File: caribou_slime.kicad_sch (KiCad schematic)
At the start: 36 parts, among them J1 BATT JST, Q1 AO3145, U1 ESP32-C3_SUPERMINI, U2 BMI270, U3 FS312F-G, U4 FS8205A, U5 TP4056, U6 ME6211C33M5G

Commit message: fix(pcb): Move S1A to enable pin of regulator
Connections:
- net VUNREG: now also S1.2 (B); no longer S1.1 (A)
- net at U6.3 (EN): now also S1.1 (A); no longer S1.2 (B)
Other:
- moved on the sheet: S1A

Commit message: fix(schematic): Add pulldown to regulator EN pin
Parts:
- added R17: 10k, Resistor_SMD:R_0805_2012Metric, symbol Device:R
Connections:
- net GND: now also R17.2
- net at S1.1 (A), U6.3 (EN): now also R17.1
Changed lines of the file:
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@@
   (junction (at 252.73 93.98) (diameter 0) (color 0 0 0 0)
   )
+  (junction (at 234.95 82.55) (diameter 0) (color 0 0 0 0)
+  )
   (junction (at 48.26 161.29) (diameter 0) (color 0 0 0 0)
   )
@@
   )
   (junction (at 113.03 143.51) (diameter 0) (color 0 0 0 0)
+  )
+  (junction (at 247.65 72.39) (diameter 0) (color 0 0 0 0)
   )
   (no_connect (at 77.47 171.45))
@@
     (stroke (width 0) (type default))
   )
+  (wire (pts (xy 247.65 72.39) (xy 234.95 72.39))
+    (stroke (width 0) (type default))
+  )
   (wire (pts (xy 72.39 153.67) (xy 77.47 153.67))
     (stroke (width 0) (type default))
@@
     (stroke (width 0) (type default))
   )
+  (wire (pts (xy 234.95 81.28) (xy 234.95 82.55))
+    (stroke (width 0) (type default))
+  )
   (wire (pts (xy 16.51 81.28) (xy 53.34 81.28))
     (stroke (width 0) (type default))
@@
   )
   (wire (pts (xy 154.94 71.12) (xy 154.94 72.39))
+    (stroke (width 0) (type default))
+  )
+  (wire (pts (xy 234.95 72.39) (xy 234.95 73.66))
     (stroke (width 0) (type default))
   )
@@
         )
       )
+    )
+  )
+  (symbol (lib_id "Device:R") (at 234.95 77.47 0) (mirror y) (unit 1)
+    (in_bom yes) (on_board yes) (dnp no)
+    (property "Reference" "R17" (at 232.41 76.2 0)
+      (effects (font (size 1.27 1.27)) (justify left))
+    )
+    (property "Value" "10k" (at 232.41 78.74 0)
+      (effects (font (size 1.27 1.27)) (justify left))
+    )
+    (property "Footprint" "Resistor_SMD:R_0805_2012Metric" (at 236.728 77.47 90)
+      (effects (font (size 1.27 1.27)) hide)
+    )
+    (property "Datasheet" "~" (at 234.95 77.47 0)
+      (effects (font (size 1.27 1.27)) hide)
+    )
+    (pin "1")
+    (pin "2")
+    (instances
+      (project "caribou_slime"
+        (path "/61bfc64c-87c3-434a-8ade-1f9e7b05e459"
+          (reference "R17") (unit 1)
+        )
+      )

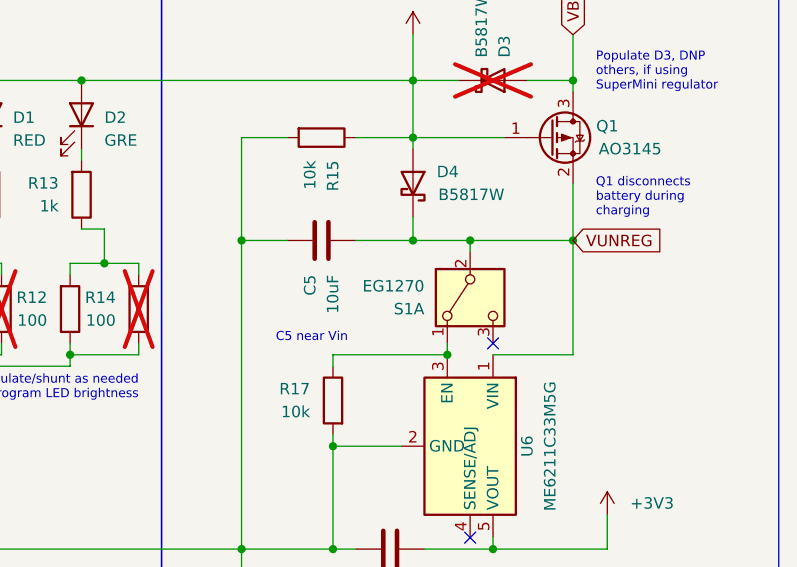
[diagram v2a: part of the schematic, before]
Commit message: refactor(schematic): Rework S1A to disconnect pulldown when reg en high
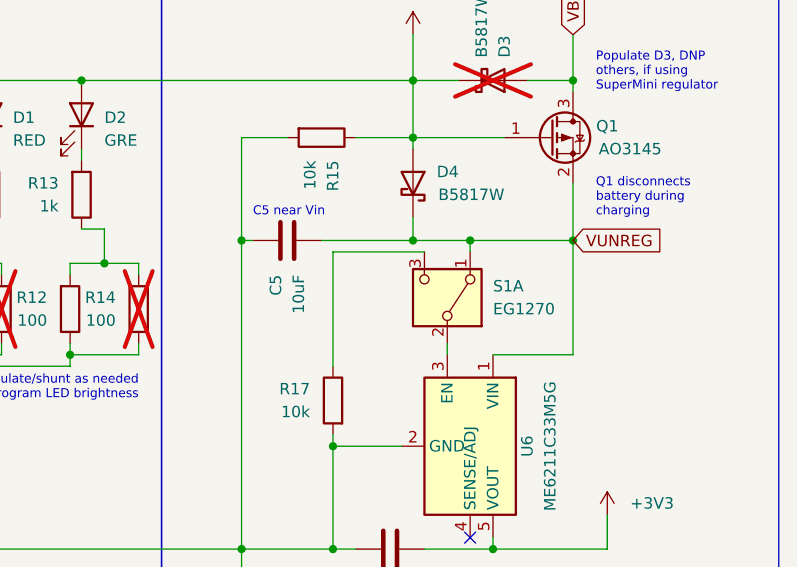
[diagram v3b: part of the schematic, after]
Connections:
- net VUNREG: now also S1.1 (A); no longer S1.2 (B)
- net at S1.3 (C): now also R17.1
- new net: S1.2 (B), U6.3 (EN)
- no-connect marks 19 -> 18
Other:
- moved on the sheet: C5, S1A
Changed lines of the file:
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@@
   (junction (at 113.03 143.51) (diameter 0) (color 0 0 0 0)
-  )
-  (junction (at 247.65 72.39) (diameter 0) (color 0 0 0 0)
   )
   (no_connect (at 77.47 171.45))
@@
   (no_connect (at 71.12 64.77))
   (no_connect (at 107.95 171.45))
-  (no_connect (at 252.73 71.12))
   (no_connect (at 71.12 57.15))
   (no_connect (at 77.47 151.13))
@@
   (no_connect (at 107.95 168.91))
   (no_connect (at 101.6 34.29))
+  (wire (pts (xy 245.11 60.96) (xy 234.95 60.96))
+    (stroke (width 0) (type default))
+  )
   (wire (pts (xy 224.79 59.69) (xy 224.79 93.98))
     (stroke (width 0) (type default))
@@
     (stroke (width 0) (type default))
   )
-  (wire (pts (xy 247.65 72.39) (xy 234.95 72.39))
-    (stroke (width 0) (type default))
-  )
   (wire (pts (xy 72.39 153.67) (xy 77.47 153.67))
     (stroke (width 0) (type default))
@@
     (stroke (width 0) (type default))
   )
-  (wire (pts (xy 243.84 59.69) (xy 237.49 59.69))
+  (wire (pts (xy 243.84 59.69) (xy 233.68 59.69))
     (stroke (width 0) (type default))
   )
@@
     (stroke (width 0) (type default))
   )
-  (wire (pts (xy 229.87 59.69) (xy 224.79 59.69))
+  (wire (pts (xy 226.06 59.69) (xy 224.79 59.69))
     (stroke (width 0) (type default))
   )
@@
     (stroke (width 0) (type default))
   )
-  (wire (pts (xy 234.95 72.39) (xy 234.95 73.66))
+  (wire (pts (xy 234.95 60.96) (xy 234.95 73.66))
     (stroke (width 0) (type default))
   )
@@
     (effects (font (size 1 1)) (justify left bottom))
   )
-  (text "C5 near Vin" (at 228.6 71.12 0)
+  (text "C5 near Vin" (at 226.06 57.15 0)
     (effects (font (size 1 1)) (justify left bottom))
   )
@@
     )
   )
-  (symbol (lib_id "Device:C") (at 233.68 59.69 90) (mirror x) (unit 1)
-    (in_bom yes) (on_board yes) (dnp no) (fields_autoplaced)
-    (property "Reference" "C5" (at 232.41 63.5 0)
+  (symbol (lib_id "Device:C") (at 229.87 59.69 90) (mirror x) (unit 1)
+    (in_bom yes) (on_board yes) (dnp no) (fields_autoplaced)
+    (property "Reference" "C5" (at 228.6 63.5 0)
       (effects (font (size 1.27 1.27)) (justify left))
     )
-    (property "Value" "10uF" (at 234.95 63.5 0)
+    (property "Value" "10uF" (at 231.14 63.5 0)
       (effects (font (size 1.27 1.27)) (justify left))
     )
-    (property "Footprint" "Capacitor_SMD:C_0805_2012Metric" (at 237.49 60.6552 0)
-      (effects (font (size 1.27 1.27)) hide)
-    )
-    (property "Datasheet" "~" (at 233.68 59.69 0)
+    (property "Footprint" "Capacitor_SMD:C_0805_2012Metric" (at 233.68 60.6552 0)
+      (effects (font (size 1.27 1.27)) hide)
+    )
+    (property "Datasheet" "~" (at 229.87 59.69 0)
       (effects (font (size 1.27 1.27)) hide)
     )
@@
     )
   )
-  (symbol (lib_id "Switch:SW_DPDT_x2") (at 250.19 66.04 90) (mirror x) (unit 1)
+  (symbol (lib_id "Switch:SW_DPDT_x2") (at 247.65 66.04 270) (mirror x) (unit 1)
     (in_bom yes) (on_board yes) (dnp no)
-    (property "Reference" "S1" (at 245.11 67.31 90)
+    (property "Reference" "S1" (at 252.73 64.77 90)
       (effects (font (size 1.27 1.27)) (justify left))
     )
-    (property "Value" "EG1270" (at 245.11 64.77 90)
+    (property "Value" "EG1270" (at 252.73 67.31 90)
       (effects (font (size 1.27 1.27)) (justify left))
     )
-    (property "Footprint" "EG1270:SW_EG1270" (at 250.19 66.04 0)
-      (effects (font (size 1.27 1.27)) hide)
-    )
-    (property "Datasheet" "~" (at 250.19 66.04 0)
-      (effects (font (size 1.27 1.27)) hide)
-    )
+    (property "Footprint" "EG1270:SW_EG1270" (at 247.65 66.04 0)
+      (effects (font (size 1.27 1.27)) hide)
+    )
+    (property "Datasheet" "~" (at 247.65 66.04 0)
+      (effects (font (size 1.27 1.27)) hide)
+    )

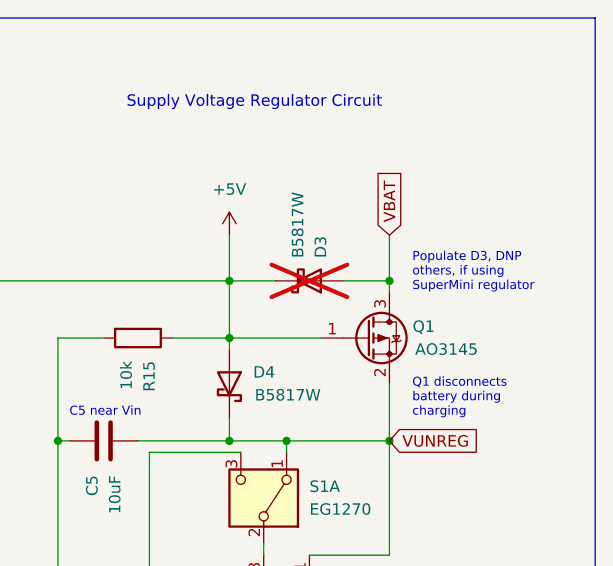
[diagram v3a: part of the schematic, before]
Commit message: chore(schematic): Remove spurious D3 (SuperMini reg has not been usable since e673114ec8c1bcd027ae6eac0da885c535fbe167 )
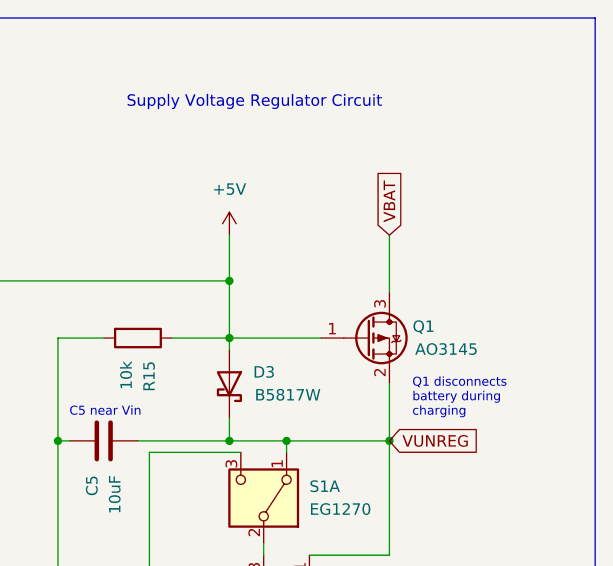
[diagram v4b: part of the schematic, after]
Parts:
- removed D3: B5817W, Diode_SMD:D_0805_2012Metric, symbol Device:D_Schottky
- renumbered D4 to D3
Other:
- note removed: "Populate D3, DNP others, if using SuperMini regulator"
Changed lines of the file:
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@@
   (junction (at 96.52 39.37) (diameter 0) (color 0 0 0 0)
-  )
-  (junction (at 261.62 41.91) (diameter 0) (color 0 0 0 0)
   )
   (junction (at 154.94 93.98) (diameter 0) (color 0 0 0 0)
@@
     (stroke (width 0) (type default))
   )
-  (wire (pts (xy 256.54 41.91) (xy 261.62 41.91))
-    (stroke (width 0) (type default))
-  )
   (wire (pts (xy 157.48 50.8) (xy 165.1 50.8))
     (stroke (width 0) (type default))
@@
     (stroke (width 0) (type default))
   )
-  (wire (pts (xy 243.84 41.91) (xy 248.92 41.91))
-    (stroke (width 0) (type default))
-  )
   (wire (pts (xy 72.39 146.05) (xy 72.39 153.67))
     (stroke (width 0) (type default))
@@
     (stroke (width 0) (type default))
   )
-  (wire (pts (xy 261.62 36.83) (xy 261.62 41.91))
+  (wire (pts (xy 261.62 36.83) (xy 261.62 43.18))
     (stroke (width 0) (type default))
   )
@@
   )
   (wire (pts (xy 234.95 93.98) (xy 237.49 93.98))
-    (stroke (width 0) (type default))
-  )
-  (wire (pts (xy 261.62 41.91) (xy 261.62 43.18))
     (stroke (width 0) (type default))
   )
@@
   (text "ESP32-C3 Circuit" (at 46.99 19.05 0)
     (effects (font (size 1.27 1.27)) (justify left bottom))
-  )
-  (text "Populate D3, DNP \nothers, if using\nSuperMini regulator"
-    (at 264.16 43.18 0)
-    (effects (font (size 1 1)) (justify left bottom))
   )
   (text "Battery Charging Circuit" (at 187.96 22.86 0)
@@
     )
   )
-  (symbol (lib_id "Device:D_Schottky") (at 252.73 41.91 0) (mirror x) (unit 1)
-    (in_bom yes) (on_board yes) (dnp yes)
-    (property "Reference" "D3" (at 254 39.37 90)
-      (effects (font (size 1.27 1.27)) (justify right))
-    )
-    (property "Value" "B5817W" (at 251.46 39.37 90)
-      (effects (font (size 1.27 1.27)) (justify right))
-    )
-    (property "Footprint" "Diode_SMD:D_0805_2012Metric" (at 252.73 41.91 0)
-      (effects (font (size 1.27 1.27)) hide)
-    )
-    (property "Datasheet" "~" (at 252.73 41.91 0)
-      (effects (font (size 1.27 1.27)) hide)
-    )
-    (property "Sim.Device" "D" (at 252.73 41.91 0)
-      (effects (font (size 1.27 1.27)) hide)
-    )
-    (property "Sim.Pins" "1=K 2=A" (at 252.73 41.91 0)
-      (effects (font (size 1.27 1.27)) hide)
-    )
-    (pin "2")
-    (pin "1")
-    (instances
-      (project "caribou_slime"
-        (path "/61bfc64c-87c3-434a-8ade-1f9e7b05e459"
-          (reference "D3") (unit 1)
-        )
-      )
-    )
-  )
   (symbol (lib_id "Device:LED") (at 207.01 45.72 270) (mirror x) (unit 1)
     (in_bom yes) (on_board yes) (dnp no) (fields_autoplaced)
@@
   (symbol (lib_id "Device:D_Schottky") (at 243.84 53.34 270) (mirror x) (unit 1)
     (in_bom yes) (on_board yes) (dnp no)
-    (property "Reference" "D4" (at 248.92 52.07 90)
+    (property "Reference" "D3" (at 248.92 52.07 90)
       (effects (font (size 1.27 1.27)) (justify right))
     )
@@
       (project "caribou_slime"
         (path "/61bfc64c-87c3-434a-8ade-1f9e7b05e459"
-          (reference "D4") (unit 1)
-        )
-      )
+          (reference "D3") (unit 1)
+        )
+      )

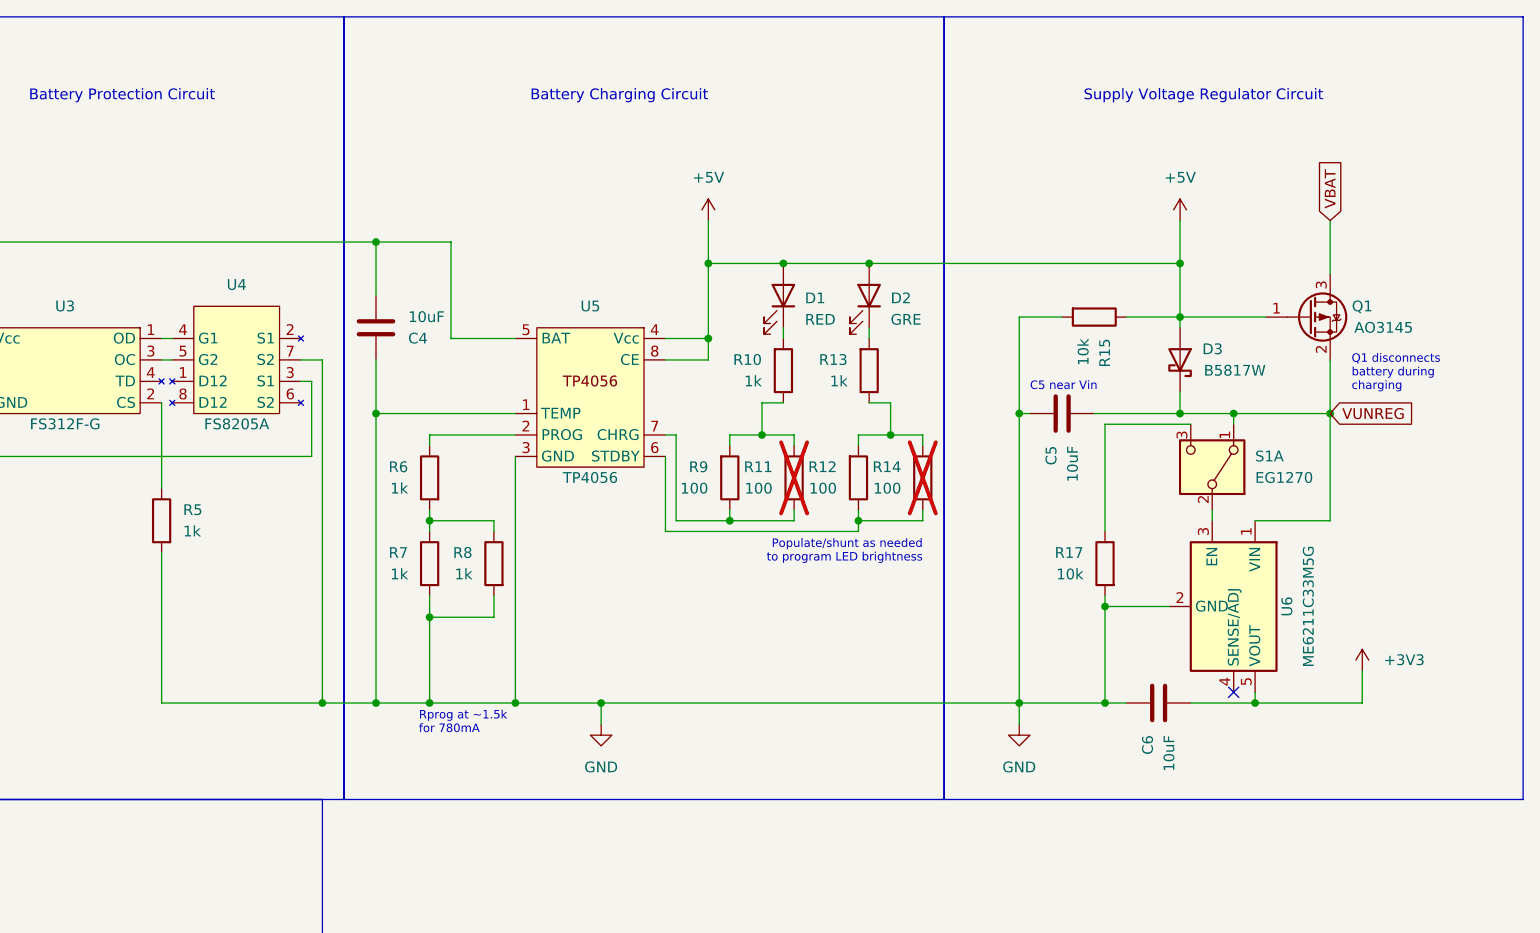
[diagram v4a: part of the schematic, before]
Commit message: chore(schematic): Clean up regulator schematic
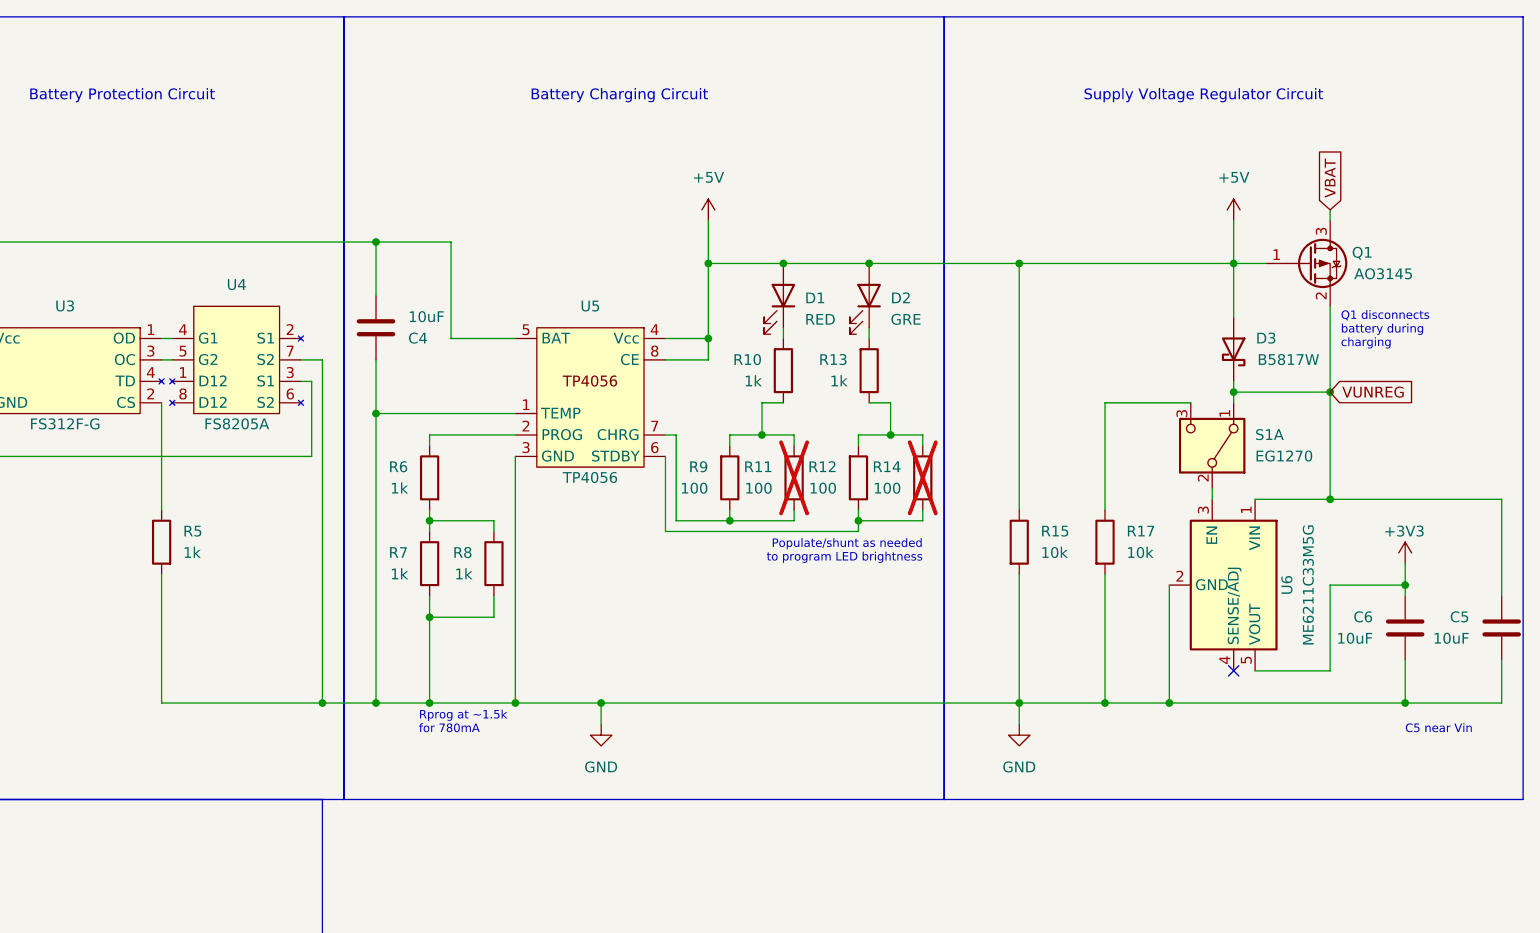
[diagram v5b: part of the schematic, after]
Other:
- moved on the sheet: C5, C6, D3, Q1, R15, R5, S1A, U6
